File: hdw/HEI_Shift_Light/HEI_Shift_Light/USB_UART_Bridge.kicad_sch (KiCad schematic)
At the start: 27 parts, among them U1304 ISO7321C

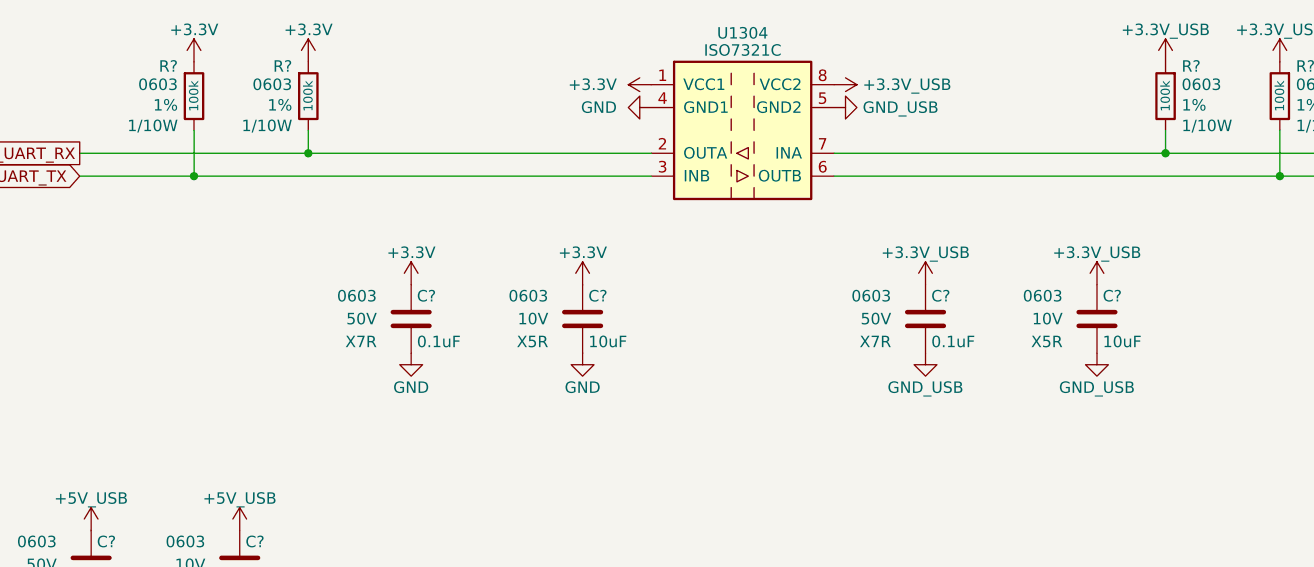
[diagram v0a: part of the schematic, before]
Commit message: populated input protection circuit passive components, updated PIC pinout, added stuff to frequency to voltage converter circuit
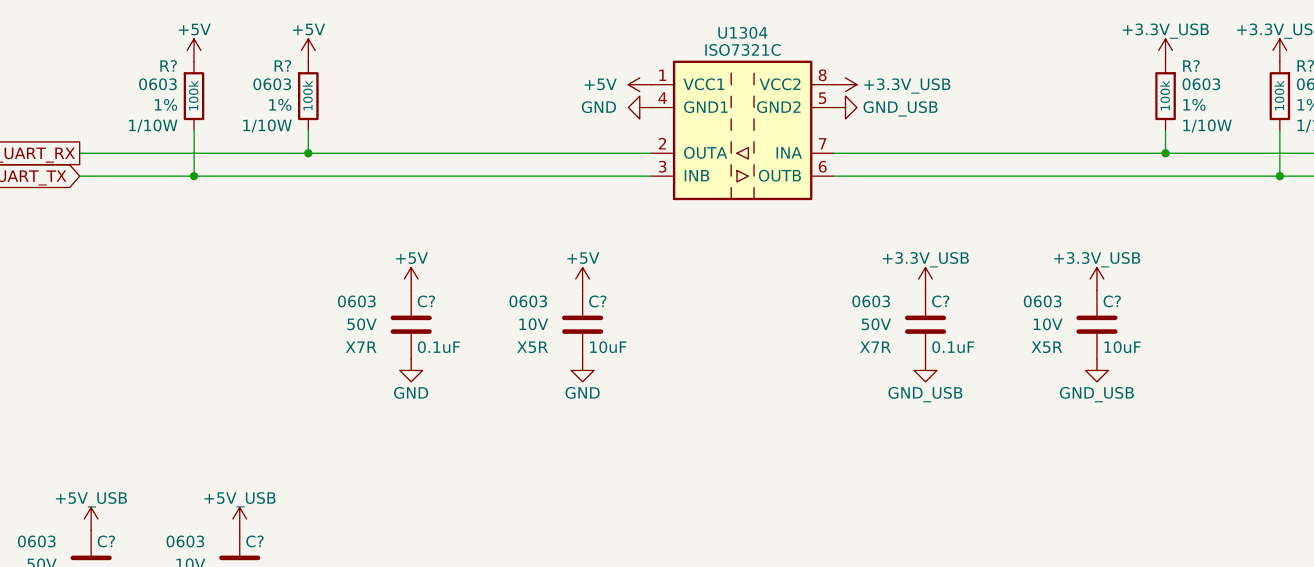
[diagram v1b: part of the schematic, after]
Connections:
- net +3.3V renamed +5V
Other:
- moved on the sheet: C?

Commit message: added more shit, RGD LED, LC input filter
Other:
- title: Nixie Clock Redux Core Board -> HEI Shift Light
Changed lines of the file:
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@@
 	(paper "A")
 	(title_block
-		(title "Nixie Clock Redux Core Board")
-		(date "2023-12-25")
-		(rev "B")
+		(title "HEI Shift Light")
+		(date "2026-05-29")
+		(rev "A")
 		(company "Drew Maatman")
 	)
@@
 		(in_pos_files yes)
 		(dnp no)
-		(property "Reference" "#FLG01303"
+		(property "Reference" "#FLG?"
 			(at 80.01 97.155 0)
 			(hide yes)
@@
 			(project "HEI_Shift_Light"
 				(path "/288c8230-69eb-4ad9-929d-f4630114196f/c4b824f9-827e-4368-b456-592a65eed557"
-					(reference "#FLG01303")
+					(reference "#FLG?")
 					(unit 1)
 				)
@@
 		(in_pos_files yes)
 		(dnp no)
-		(property "Reference" "#PWR018"
+		(property "Reference" "#PWR?"
 			(at 196.85 125.73 0)
 			(hide yes)
@@
 			(project "HEI_Shift_Light"
 				(path "/288c8230-69eb-4ad9-929d-f4630114196f/c4b824f9-827e-4368-b456-592a65eed557"
-					(reference "#PWR018")
+					(reference "#PWR?")
 					(unit 1)
 				)
@@
 		(in_pos_files yes)
 		(dnp no)
-		(property "Reference" "#PWR024"
+		(property "Reference" "#PWR?"
 			(at 116.84 53.34 0)
 			(hide yes)
@@
 			(project "HEI_Shift_Light"
 				(path "/288c8230-69eb-4ad9-929d-f4630114196f/c4b824f9-827e-4368-b456-592a65eed557"
-					(reference "#PWR024")
+					(reference "#PWR?")
 					(unit 1)
 				)
@@
 		(in_pos_files yes)
 		(dnp no)
-		(property "Reference" "#PWR017"
+		(property "Reference" "#PWR?"
 			(at 209.55 125.73 0)
 			(hide yes)
@@
 			(project "HEI_Shift_Light"
 				(path "/288c8230-69eb-4ad9-929d-f4630114196f/c4b824f9-827e-4368-b456-592a65eed557"
-					(reference "#PWR017")
+					(reference "#PWR?")
 					(unit 1)
 				)
@@
 		(in_pos_files yes)
 		(dnp no)
-		(property "Reference" "#PWR019"
+		(property "Reference" "#PWR?"
 			(at 247.65 148.59 0)
 			(hide yes)
@@
 			(project "HEI_Shift_Light"
 				(path "/288c8230-69eb-4ad9-929d-f4630114196f/c4b824f9-827e-4368-b456-592a65eed557"
-					(reference "#PWR019")
+					(reference "#PWR?")
 					(unit 1)
 				)
@@
 		(in_pos_files yes)
 		(dnp no)
-		(property "Reference" "#PWR021"
+		(property "Reference" "#PWR?"
 			(at 73.66 27.94 0)
 			(hide yes)
@@
 			(project "HEI_Shift_Light"
 				(path "/288c8230-69eb-4ad9-929d-f4630114196f/c4b824f9-827e-4368-b456-592a65eed557"
-					(reference "#PWR021")
+					(reference "#PWR?")
 					(unit 1)
 				)
@@
 		(in_pos_files yes)
 		(dnp no)
-		(property "Reference" "#PWR023"
+		(property "Reference" "#PWR?"
 			(at 97.79 53.34 0)
 			(hide yes)
@@
 			(project "HEI_Shift_Light"
 				(path "/288c8230-69eb-4ad9-929d-f4630114196f/c4b824f9-827e-4368-b456-592a65eed557"
-					(reference "#PWR023")
+					(reference "#PWR?")
 					(unit 1)
 				)
@@
 		(in_pos_files yes)
 		(dnp no)
-		(property "Reference" "#PWR01310"
+		(property "Reference" "#PWR?"
 			(at 120.65 127 0)
 			(hide yes)
@@
 			(project "HEI_Shift_Light"
 				(path "/288c8230-69eb-4ad9-929d-f4630114196f/c4b824f9-827e-4368-b456-592a65eed557"
-					(reference "#PWR01310")
+					(reference "#PWR?")
 					(unit 1)
 				)
@@
 		(in_pos_files yes)
 		(dnp no)
-		(property "Reference" "#PWR01311"
+		(property "Reference" "#PWR?"
 			(at 92.71 127 0)
 			(hide yes)
@@
 			(project "HEI_Shift_Light"
 				(path "/288c8230-69eb-4ad9-929d-f4630114196f/c4b824f9-827e-4368-b456-592a65eed557"
-					(reference "#PWR01311")
+					(reference "#PWR?")
 					(unit 1)
 				)
@@
 		(in_pos_files yes)
 		(dnp no)
-		(property "Reference" "#PWR01303"
+		(property "Reference" "#PWR?"
 			(at 151.13 29.21 0)
 			(hide yes)
@@
 			(project "HEI_Shift_Light"
 				(path "/288c8230-69eb-4ad9-929d-f4630114196f/c4b824f9-827e-4368-b456-592a65eed557"
-					(reference "#PWR01303")
+					(reference "#PWR?")
 					(unit 1)
 				)
@@
 		(in_pos_files yes)
 		(dnp no)
-		(property "Reference" "#PWR01319"
+		(property "Reference" "#PWR?"
 			(at 62.23 90.17 0)
 			(hide yes)
@@
 			(project "HEI_Shift_Light"
 				(path "/288c8230-69eb-4ad9-929d-f4630114196f/c4b824f9-827e-4368-b456-592a65eed557"
-					(reference "#PWR01319")
+					(reference "#PWR?")
 					(unit 1)
 				)
@@
 		(in_pos_files yes)
 		(dnp no)
-		(property "Reference" "#PWR01341"
+		(property "Reference" "#PWR?"
 			(at 154.94 63.5 0)
 			(hide yes)
@@
 			(project "HEI_Shift_Light"
 				(path "/288c8230-69eb-4ad9-929d-f4630114196f/c4b824f9-827e-4368-b456-592a65eed557"
-					(reference "#PWR01341")
+					(reference "#PWR?")
 					(unit 1)
 				)
@@
 		(in_pos_files yes)
 		(dnp no)
-		(property "Reference" "#PWR01346"
+		(property "Reference" "#PWR?"
 			(at 97.79 63.5 0)
 			(hide yes)
@@
 			(project "HEI_Shift_Light"
 				(path "/288c8230-69eb-4ad9-929d-f4630114196f/c4b824f9-827e-4368-b456-592a65eed557"
-					(reference "#PWR01346")
+					(reference "#PWR?")
 					(unit 1)
 				)
@@
 		(in_pos_files yes)
 		(dnp no)
-		(property "Reference" "#PWR016"
+		(property "Reference" "#PWR?"
 			(at 240.03 135.89 0)
 			(hide yes)
@@
 			(project "HEI_Shift_Light"
 				(path "/288c8230-69eb-4ad9-929d-f4630114196f/c4b824f9-827e-4368-b456-592a65eed557"
-					(reference "#PWR016")
+					(reference "#PWR?")
 					(unit 1)
 				)
@@
 		(in_pos_files yes)
 		(dnp no)
-		(property "Reference" "#PWR020"
+		(property "Reference" "#PWR?"
 			(at 156.21 128.27 0)
 			(hide yes)
@@
 			(project "HEI_Shift_Light"
 				(path "/288c8230-69eb-4ad9-929d-f4630114196f/c4b824f9-827e-4368-b456-592a65eed557"
-					(reference "#PWR020")
+					(reference "#PWR?")
 					(unit 1)
 				)
@@
 		(in_pos_files yes)
 		(dnp no)
-		(property "Reference" "#PWR01309"
+		(property "Reference" "#PWR?"
 			(at 142.24 127 0)
 			(hide yes)
@@
 			(project "HEI_Shift_Light"
 				(path "/288c8230-69eb-4ad9-929d-f4630114196f/c4b824f9-827e-4368-b456-592a65eed557"
-					(reference "#PWR01309")
+					(reference "#PWR?")
 					(unit 1)
 				)
@@
 		(in_pos_files yes)
 		(dnp no)
-		(property "Reference" "U1304"
+		(property "Reference" "U?"
 			(at 134.62 20.955 0)
 			(show_name no)
@@
 			(project "HEI_Shift_Light"
 				(path "/288c8230-69eb-4ad9-929d-f4630114196f/c4b824f9-827e-4368-b456-592a65eed557"
-					(reference "U1304")
+					(reference "U?")
 					(unit 1)
 				)
@@
 		(in_pos_files yes)
 		(dnp no)
-		(property "Reference" "#PWR01305"
+		(property "Reference" "#PWR?"
 			(at 184.15 125.73 0)
 			(hide yes)
@@
 			(project "HEI_Shift_Light"
 				(path "/288c8230-69eb-4ad9-929d-f4630114196f/c4b824f9-827e-4368-b456-592a65eed557"
-					(reference "#PWR01305")
+					(reference "#PWR?")
 					(unit 1)
 				)
@@
 		(in_pos_files yes)
 		(dnp no)
-		(property "Reference" "#PWR01320"
+		(property "Reference" "#PWR?"
 			(at 44.45 90.17 0)
 			(hide yes)
@@
 			(project "HEI_Shift_Light"
 				(path "/288c8230-69eb-4ad9-929d-f4630114196f/c4b824f9-827e-4368-b456-592a65eed557"
-					(reference "#PWR01320")
+					(reference "#PWR?")
 					(unit 1)
 				)
@@
 		(in_pos_files yes)
 		(dnp no)
-		(property "Reference" "#PWR022"
+		(property "Reference" "#PWR?"
 			(at 86.36 27.94 0)
 			(hide yes)
@@
 			(project "HEI_Shift_Light"
 				(path "/288c8230-69eb-4ad9-929d-f4630114196f/c4b824f9-827e-4368-b456-592a65eed557"
-					(reference "#PWR022")
+					(reference "#PWR?")
 					(unit 1)
 				)
@@
 		(dnp no)
 		(fields_autoplaced yes)
-		(property "Reference" "#PWR025"
+		(property "Reference" "#PWR?"
 			(at 128.27 26.67 0)
 			(hide yes)
@@
 			(project "HEI_Shift_Light"
 				(path "/288c8230-69eb-4ad9-929d-f4630114196f/c4b824f9-827e-4368-b456-592a65eed557"
-					(reference "#PWR025")
+					(reference "#PWR?")
 					(unit 1)
 				)
@@
 		(in_pos_files yes)
 		(dnp no)
-		(property "Reference" "#PWR01343"
+		(property "Reference" "#PWR?"
 			(at 173.99 63.5 0)
 			(hide yes)
@@
 			(project "HEI_Shift_Light"
 				(path "/288c8230-69eb-4ad9-929d-f4630114196f/c4b824f9-827e-4368-b456-592a65eed557"
-					(reference "#PWR01343")
+					(reference "#PWR?")
 					(unit 1)
 				)
@@
 		(in_pos_files yes)
 		(dnp no)
-		(property "Reference" "#PWR01313"
+		(property "Reference" "#PWR?"
 			(at 53.34 128.27 0)
 			(hide yes)
@@
 			(project "HEI_Shift_Light"
 				(path "/288c8230-69eb-4ad9-929d-f4630114196f/c4b824f9-827e-4368-b456-592a65eed557"
-					(reference "#PWR01313")
+					(reference "#PWR?")
 					(unit 1)
 				)
@@
 		(in_pos_files yes)
 		(dnp no)
-		(property "Reference" "#PWR01318"
+		(property "Reference" "#PWR?"
 			(at 78.74 90.17 0)
 			(hide yes)
@@
 			(project "HEI_Shift_Light"
 				(path "/288c8230-69eb-4ad9-929d-f4630114196f/c4b824f9-827e-4368-b456-592a65eed557"
-					(reference "#PWR01318")
+					(reference "#PWR?")
 					(unit 1)
 				)
@@
 		(in_pos_files yes)
 		(dnp no)
-		(property "Reference" "#PWR01347"
+		(property "Reference" "#PWR?"
 			(at 116.84 63.5 0)
 			(hide yes)
@@
 			(project "HEI_Shift_Light"
 				(path "/288c8230-69eb-4ad9-929d-f4630114196f/c4b824f9-827e-4368-b456-592a65eed557"
-					(reference "#PWR01347")
+					(reference "#PWR?")
 					(unit 1)
 				)
@@
 		(in_pos_files yes)
 		(dnp no)
-		(property "Reference" "#PWR01302"
+		(property "Reference" "#PWR?"
 			(at 118.11 29.21 0)
 			(hide yes)
@@
 			(project "HEI_Shift_Light"
 				(path "/288c8230-69eb-4ad9-929d-f4630114196f/c4b824f9-827e-4368-b456-592a65eed557"
-					(reference "#PWR01302")
+					(reference "#PWR?")
 					(unit 1)
 				)
